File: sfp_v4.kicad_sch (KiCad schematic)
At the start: 78 parts

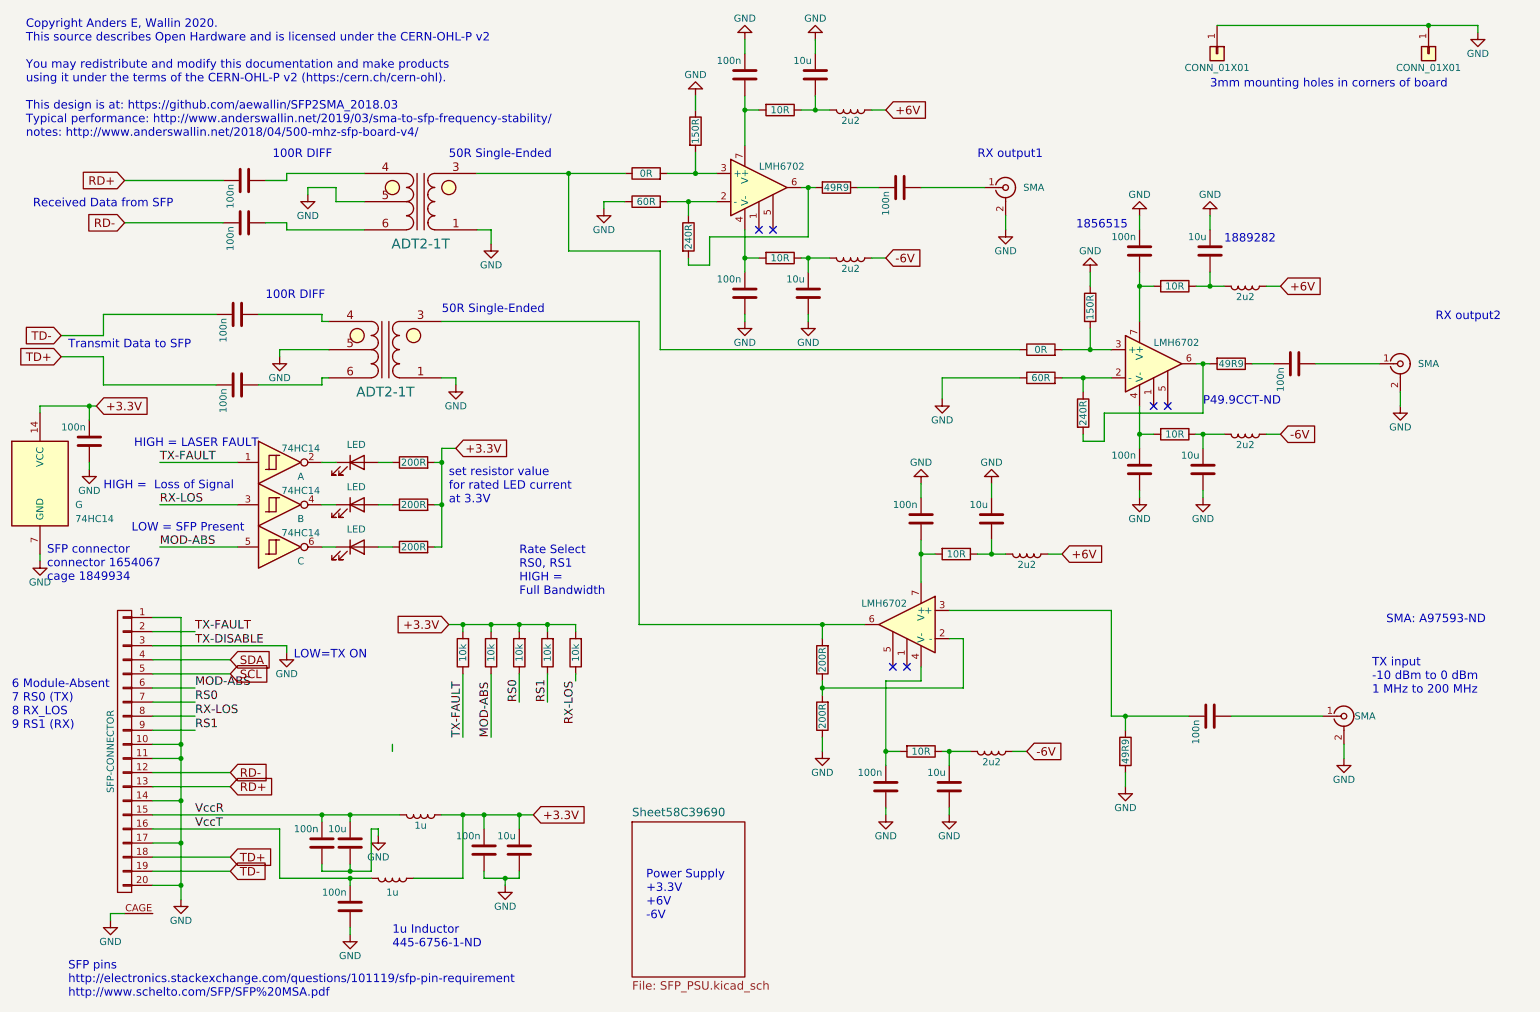
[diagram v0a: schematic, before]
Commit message: update to kicad 9
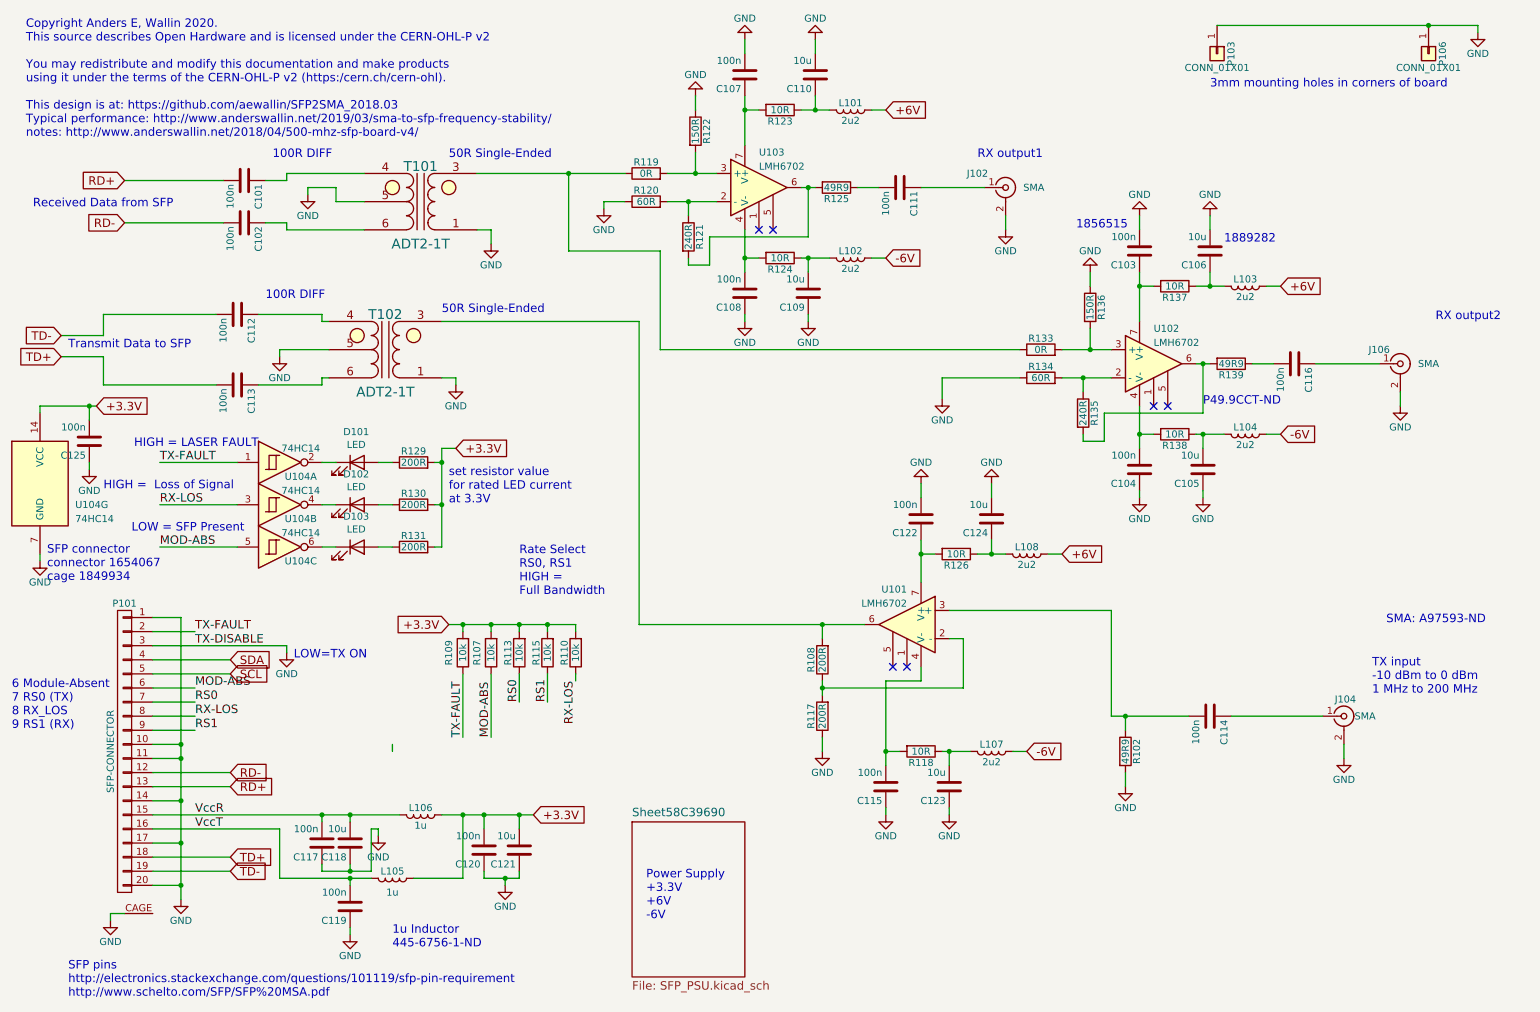
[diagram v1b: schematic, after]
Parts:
- gave numbers to parts that had none: 75
